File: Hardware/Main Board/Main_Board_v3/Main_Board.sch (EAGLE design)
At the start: 51 parts, among them IC1 MBED_MICROCONTROLLER, IC2 NE555, Q1 IRF3704, Q2 BS170

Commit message: Changed mounting holes and SD card Power pin
1. The mounting holes locations have been changed slightly so that they
are to the nearest mm
2. The SD card can be power gated using pin 9.
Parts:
- removed 2N7000: (no value), jumper:JP2E
- removed C2: 100nF, capacitor-wima:C5/3
- removed JP10: (no value), jumper:JP1E
- removed JP9: JP9, jumper:JP1E
- removed POWER_SUPPLY: TRACO_ISOLATED_SUPPLY, ekohub2013:TRACO_ISOLATED_SUPPLY
- removed U$2: MICROSD_SOCKET, ekohub2013:MICROSD_SOCKET
- removed U$3: PANASONIC_CR2032, Datalogging_Custom_Parts:PANASONIC_CR2032
- added C11: 100nF, capacitor-wima:C5/3.5
- added JP15, JP16, JP17, JP18, JP19, JP20: (no value), jumper:JP4E
- added JP5: (no value), jumper:JP1E
- added Q3, Q4, Q6: IRF3704L-V, transistor-power:IRF3704L-V
- added Q5: BS170, transistor-small-signal:BS170
- added R17: 20, rcl:R-EU_0411/12
- added R18: (no value), rcl:R-EU_0411/12
- added R19: 1M, rcl:R-EU_0411/12
- added R5: (no value), rcl:R-TRIMM
- added U$9: TRACO_ISOLATED_SUPPLY, ekohub2013:TRACO_ISOLATED_SUPPLY
- C1, C3, C4, C5, C6, C7, C8, C9: device capacitor-wima:C5/3 -> capacitor-wima:C5/3.5
- C10: value (none) -> 10n; device capacitor-wima:C5/3 -> capacitor-wima:C5/3.5
- DIS1: device display-lcd:TUXGR_16X2_R2 -> display-lcd3:TUXGR_16X2_R2
- JP1: value JP1 -> (none); device jumper:JP10Q -> jumper:JP2W
- JP2: value JP2 -> (none); device jumper:JP10Q -> jumper:JP2W
- JP3: value JP3 -> (none); device jumper:JP10Q -> jumper:JP4E
- JP4: value JP4 -> (none); device jumper:JP10Q -> jumper:JP4E
- Q1: value IRF3704 -> BS170; device transistor-power:IRF3704 -> transistor-small-signal:BS170
- R13, R6: value (none) -> 1M
- R4: value (none) -> 300k
- R7: value 20 -> (none)
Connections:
- removed net 5V: Q1.S, R13.2
- removed net N$10: IC1.P$10, JP1.1, JP1.2
- removed net N$13: IC1.P$13, JP2.15, JP2.16
- removed net N$14: IC1.P$14, JP2.13, JP2.14
- removed net N$23: IC1.P$38, JP4.15, JP4.16
- removed net N$24: IC1.P$37, JP4.13, JP4.14
- removed net N$35: IC1.P$26, JP3.11, JP3.12
- removed net N$36: IC1.P$25, JP3.10, JP3.9
- removed net N$45: DIS1.NC@1, R7.2
- removed net NR: IC1.P$4, JP1.13, JP1.14
- removed net P16_LCD: 2N7000.1, DIS1.NC@2
- removed net P29: IC1.P$29, IC2.TRI, JP3.17, JP3.18
- removed net P33: C3.1, IC1.P$33, JP4.5, JP4.6, R1.2, U$5.1
- removed net P34: C4.1, IC1.P$34, JP4.7, JP4.8, R14.2, U$6.1
- removed net P35: C5.1, IC1.P$35, JP4.10, JP4.9, R15.2, U$7.1
- removed net P36: IC1.P$36, JP4.11, JP4.12, Q2.G
- removed net VB: IC1.P$3, JP1.15, JP1.16, U$3.VB
- new net 3V3: JP2.1, Q6.D
- new net N$8: Q1.D, Q4.G, R6.1
- new net P10: C3.1, IC1.P$10, R1.2, U$5.1
- new net P11: C4.1, IC1.P$11, R14.2, U$6.1
- new net P12: C5.1, IC1.P$12, R15.2, U$7.1
- new net P13: C6.1, IC1.P$13, R16.2, U$8.1
- new net P14: IC1.P$14, IC2.TRI
- new net P9: IC1.P$9, Q5.G
- net 3V3_MBED: now also C11.2, Q6.S, R19.2; no longer C2.1, JP4.19, JP4.20, U$2.VDD
- net 5V_MBED: now also JP5.1; no longer C1.1, D1.A, DIS1.VCC, IC2./RES, IC2.VCC+, JP10.1, JP4.17, JP4.18, R4.2, R7.1, U$5.4, U$6.4, U$7.4, U$8.4
- net D+: no longer JP4.1, JP4.2
- net D-: no longer JP4.3, JP4.4
- net GND: now also C11.1, DIS1.NC@2, JP1.2, JP15.2, JP16.2, JP17.2, JP18.2, JP19.2, JP20.2, JP3.2, JP4.2, Q1.S, Q5.S, R5.A, R5.S, U$9.VOUT-; no longer 2N7000.3, C2.2, JP1.19, JP1.20, JP10.2, POWER_SUPPLY.VOUT-, R6.1, U$2.VSS, U$3.GND
- net MODEM: now also Q3.D; no longer Q1.D
- net N$11: now also IC2.OUT, Q1.G; no longer IC1.P$11, JP2.19, JP2.20
- net N$12: now also Q4.D, R17.2; no longer IC1.P$12, JP2.17, JP2.18
- net N$3: now also R5.E; no longer R6.2
- net N$5: now also Q3.G; no longer Q1.G
- net N$7: now also Q5.D, Q6.G, R19.1; no longer 2N7000.2, IC2.OUT
- net N$9: now also DIS1.NC@1, R17.1; no longer IC1.P$9, JP1.3, JP1.4
- net P15: no longer JP2.11, JP2.12
- net P16: no longer JP2.10, JP2.9
- net P17: no longer JP2.7, JP2.8
- net P18: no longer JP2.5, JP2.6
- net P19: no longer JP2.3, JP2.4
- net P20: no longer JP2.1, JP2.2
- net P21: no longer JP3.1, JP3.2
- net P22: no longer JP3.3, JP3.4
- net P23: no longer JP3.5, JP3.6
- net P24: no longer JP3.7, JP3.8
- net P30: now also Q2.G; no longer C6.1, JP3.19, JP3.20, R16.2, U$8.1
- net P5: now also JP2.2; no longer JP1.11, JP1.12, U$2.DI
- net P6: now also JP1.1; no longer JP1.10, JP1.9, U$2.DO
- net P7: now also JP1.3; no longer JP1.7, JP1.8, U$2.CLK
- net P8: now also JP2.3; no longer JP1.5, JP1.6, U$2.CS
- net SCL: now also JP15.4, JP16.4, JP17.4, JP18.4, JP19.4, JP20.4, JP3.4, JP4.4, R7.2; no longer JP3.13, JP3.14, JP9.2
- net SDA: now also JP15.3, JP16.3, JP17.3, JP18.3, JP19.3, JP20.3, JP3.3, JP4.3, R18.2; no longer JP3.15, JP3.16, JP9.1
- net VIN: now also C1.1, D1.A, DIS1.VCC, IC2./RES, IC2.VCC+, JP15.1, JP16.1, JP17.1, JP18.1, JP19.1, JP20.1, JP3.1, JP4.1, JP5.2, Q3.S, Q4.S, R13.2, R18.1, R4.2, R6.2, R7.1, U$5.4, U$6.4, U$7.4, U$8.4, U$9.VOUT+; no longer JP1.17, JP1.18, POWER_SUPPLY.VOUT+
- net VIN+: now also U$9.VIN1+, U$9.VIN2+; no longer POWER_SUPPLY.VIN1+, POWER_SUPPLY.VIN2+
- net VIN-: now also U$9.VIN1-, U$9.VIN2-; no longer POWER_SUPPLY.VIN1-, POWER_SUPPLY.VIN2-
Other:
- note added: "The 5V_MBED will only be powered when the USB is on"
- note added: "make holes for switches bigger"
- moved on the sheet: C1, C10, C3, C4, C5, C6, C7, C8, C9, D1, D2, D3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

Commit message: Added power control of the LCD screen
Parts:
- added Q7: BS170, transistor-small-signal:BS170
- added Q8: IRF3704L-V, transistor-power:IRF3704L-V
- added R20: 1M, rcl:R-EU_0411/12
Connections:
- new net N$10: Q7.D, Q8.G, R20.1
- new net P25: IC1.P$25, Q7.G
- new net VIN_LCD: C1.1, DIS1.VCC, Q8.D
- net GND: now also Q7.S
- net VIN: now also Q8.S, R20.2; no longer C1.1, DIS1.VCC
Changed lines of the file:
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@@
 <part name="SUPPLY8" library="supply2" deviceset="GND" device=""/>
 <part name="Q6" library="transistor-power" deviceset="IRF3704" device="L-V"/>
+<part name="Q7" library="transistor-small-signal" deviceset="BS170" device=""/>
+<part name="R20" library="rcl" deviceset="R-EU_" device="0411/12" value="1M"/>
+<part name="SUPPLY12" library="supply2" deviceset="GND" device=""/>
+<part name="Q8" library="transistor-power" deviceset="IRF3704" device="L-V"/>
 </parts>
 <sheets>
@@
 <instance part="SUPPLY8" gate="GND" x="163.83" y="-76.2"/>
 <instance part="Q6" gate="G$1" x="166.37" y="-44.45" rot="MR90"/>
+<instance part="Q7" gate="1" x="-123.19" y="-88.9"/>
+<instance part="R20" gate="G$1" x="-137.16" y="-73.66" rot="R90"/>
+<instance part="SUPPLY12" gate="GND" x="-120.65" y="-101.6"/>
+<instance part="Q8" gate="G$1" x="-118.11" y="-69.85" rot="MR90"/>
 </instances>
 <busses>
@@
 <pinref part="SUPPLY8" gate="GND" pin="GND"/>
 </segment>
+<segment>
+<pinref part="Q7" gate="1" pin="S"/>
+<wire x1="-120.65" y1="-93.98" x2="-120.65" y2="-99.06" width="0.1524" layer="91"/>
+<pinref part="SUPPLY12" gate="GND" pin="GND"/>
+</segment>
 </net>
 <net name="VIN" class="0">
@@
 <label x="76.2" y="-33.02" size="1.4224" layer="95" rot="R180"/>
 <pinref part="Q3" gate="G$1" pin="S"/>
-</segment>
-<segment>
-<wire x1="-71.12" y1="-63.5" x2="-71.12" y2="-67.31" width="0.1524" layer="91"/>
-<label x="-79.375" y="-65.405" size="0.8128" layer="95" rot="R180"/>
-<pinref part="DIS1" gate="G$1" pin="VCC"/>
-<wire x1="-71.12" y1="-67.31" x2="-80.01" y2="-67.31" width="0.1524" layer="91"/>
-<pinref part="C1" gate="G$1" pin="1"/>
-<wire x1="-80.01" y1="-67.31" x2="-80.01" y2="-82.55" width="0.1524" layer="91"/>
 </segment>
 <segment>
@@
 <wire x1="83.82" y1="20.32" x2="77.47" y2="20.32" width="0.1524" layer="91"/>
 <wire x1="77.47" y1="20.32" x2="77.47" y2="16.51" width="0.1524" layer="91"/>
+</segment>
+<segment>
+<wire x1="-123.19" y1="-67.31" x2="-137.16" y2="-67.31" width="0.1524" layer="91"/>
+<pinref part="R20" gate="G$1" pin="2"/>
+<wire x1="-137.16" y1="-67.31" x2="-146.05" y2="-67.31" width="0.1524" layer="91"/>
+<wire x1="-137.16" y1="-68.58" x2="-137.16" y2="-67.31" width="0.1524" layer="91"/>
+<junction x="-137.16" y="-67.31"/>
+<label x="-142.24" y="-64.77" size="1.4224" layer="95" rot="R180"/>
+<pinref part="Q8" gate="G$1" pin="S"/>
 </segment>
 </net>
@@
 </segment>
 </net>
+<net name="N$10" class="0">
+<segment>
+<pinref part="Q7" gate="1" pin="D"/>
+<wire x1="-120.65" y1="-72.39" x2="-120.65" y2="-81.28" width="0.1524" layer="91"/>
+<pinref part="Q8" gate="G$1" pin="G"/>
+<pinref part="R20" gate="G$1" pin="1"/>
+<wire x1="-120.65" y1="-81.28" x2="-120.65" y2="-83.82" width="0.1524" layer="91"/>
+<wire x1="-137.16" y1="-78.74" x2="-137.16" y2="-81.28" width="0.1524" layer="91"/>
+<wire x1="-137.16" y1="-81.28" x2="-120.65" y2="-81.28" width="0.1524" layer="91"/>
+<junction x="-120.65" y="-81.28"/>
+</segment>
+</net>
+<net name="VIN_LCD" class="0">
+<segment>
+<wire x1="-71.12" y1="-63.5" x2="-71.12" y2="-67.31" width="0.1524" layer="91"/>
+<label x="-79.375" y="-65.405" size="0.8128" layer="95" rot="R180"/>
+<pinref part="DIS1" gate="G$1" pin="VCC"/>
+<wire x1="-71.12" y1="-67.31" x2="-80.01" y2="-67.31" width="0.1524" layer="91"/>
+<pinref part="C1" gate="G$1" pin="1"/>
+<wire x1="-80.01" y1="-67.31" x2="-80.01" y2="-82.55" width="0.1524" layer="91"/>
+<pinref part="Q8" gate="G$1" pin="D"/>
+<wire x1="-80.01" y1="-67.31" x2="-113.03" y2="-67.31" width="0.1524" layer="91"/>
+<junction x="-80.01" y="-67.31"/>
+</segment>
+</net>
+<net name="P25" class="0">
+<segment>
+<pinref part="Q7" gate="1" pin="G"/>
+<wire x1="-128.27" y1="-88.9" x2="-135.89" y2="-88.9" width="0.1524" layer="91"/>
+<label x="-135.89" y="-90.805" size="1.4224" layer="95"/>
+</segment>
+<segment>
+<pinref part="IC1" gate="G$1" pin="P$25"/>
+<wire x1="19.05" y1="-12.7" x2="35.56" y2="-12.7" width="0.1524" layer="91"/>
+<label x="36.83" y="-12.7" size="1.778" layer="95"/>
+</segment>
+</net>

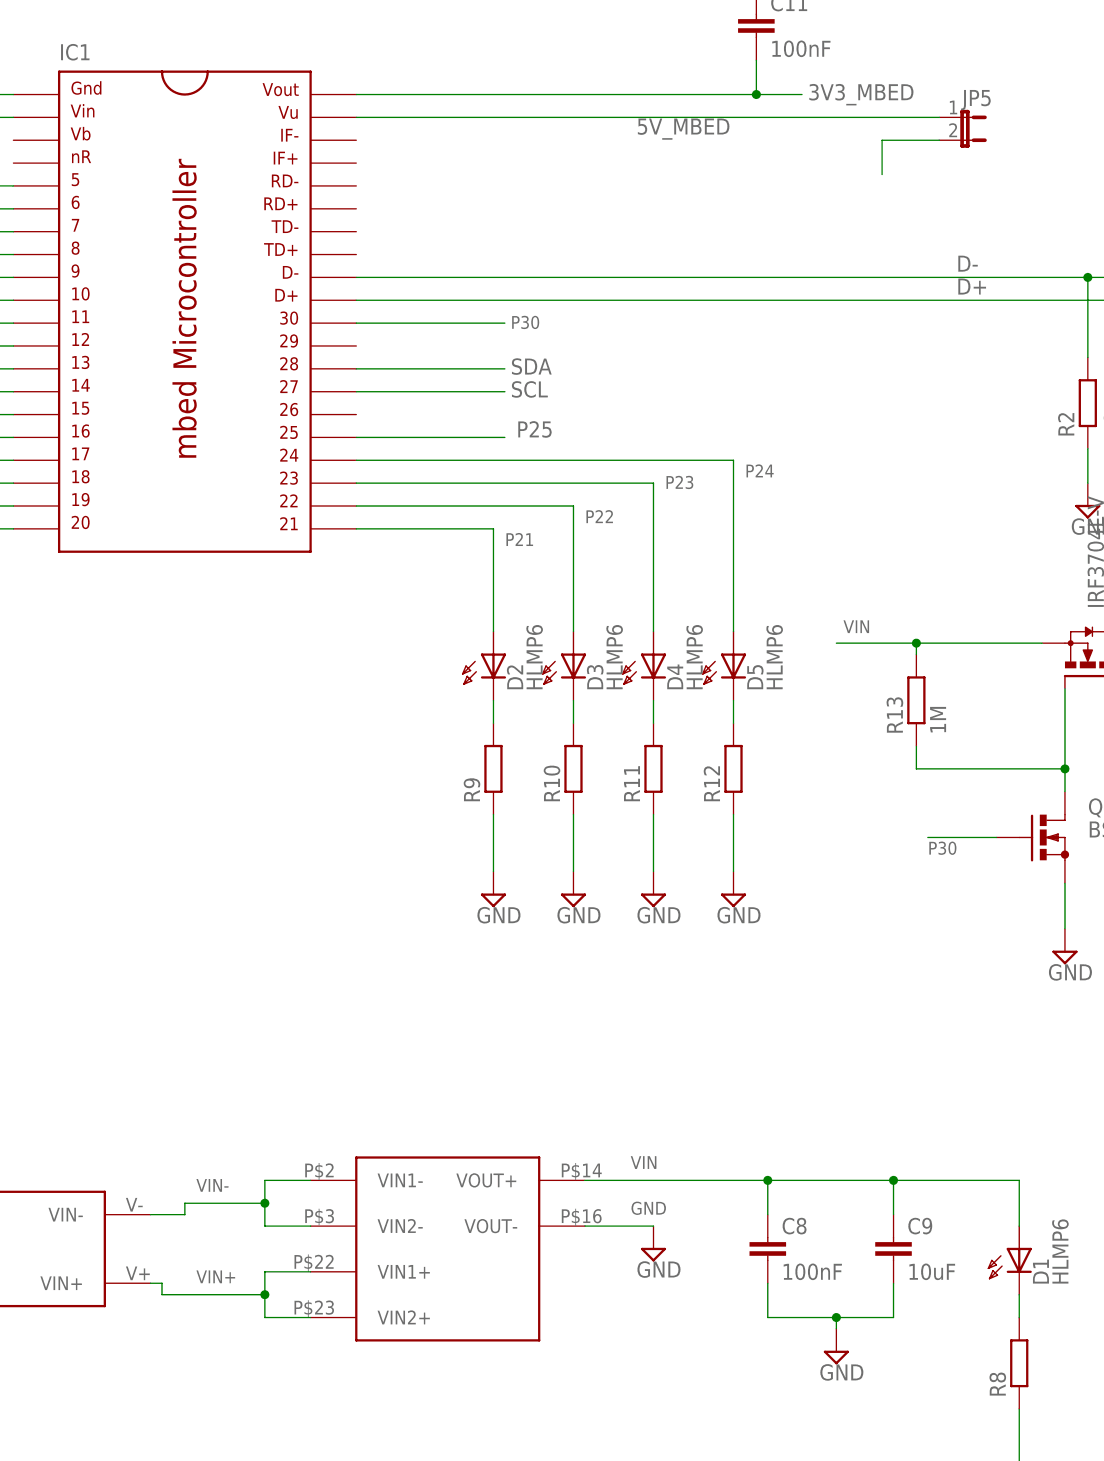
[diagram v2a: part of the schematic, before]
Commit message: Added Reverse Polarity Protection
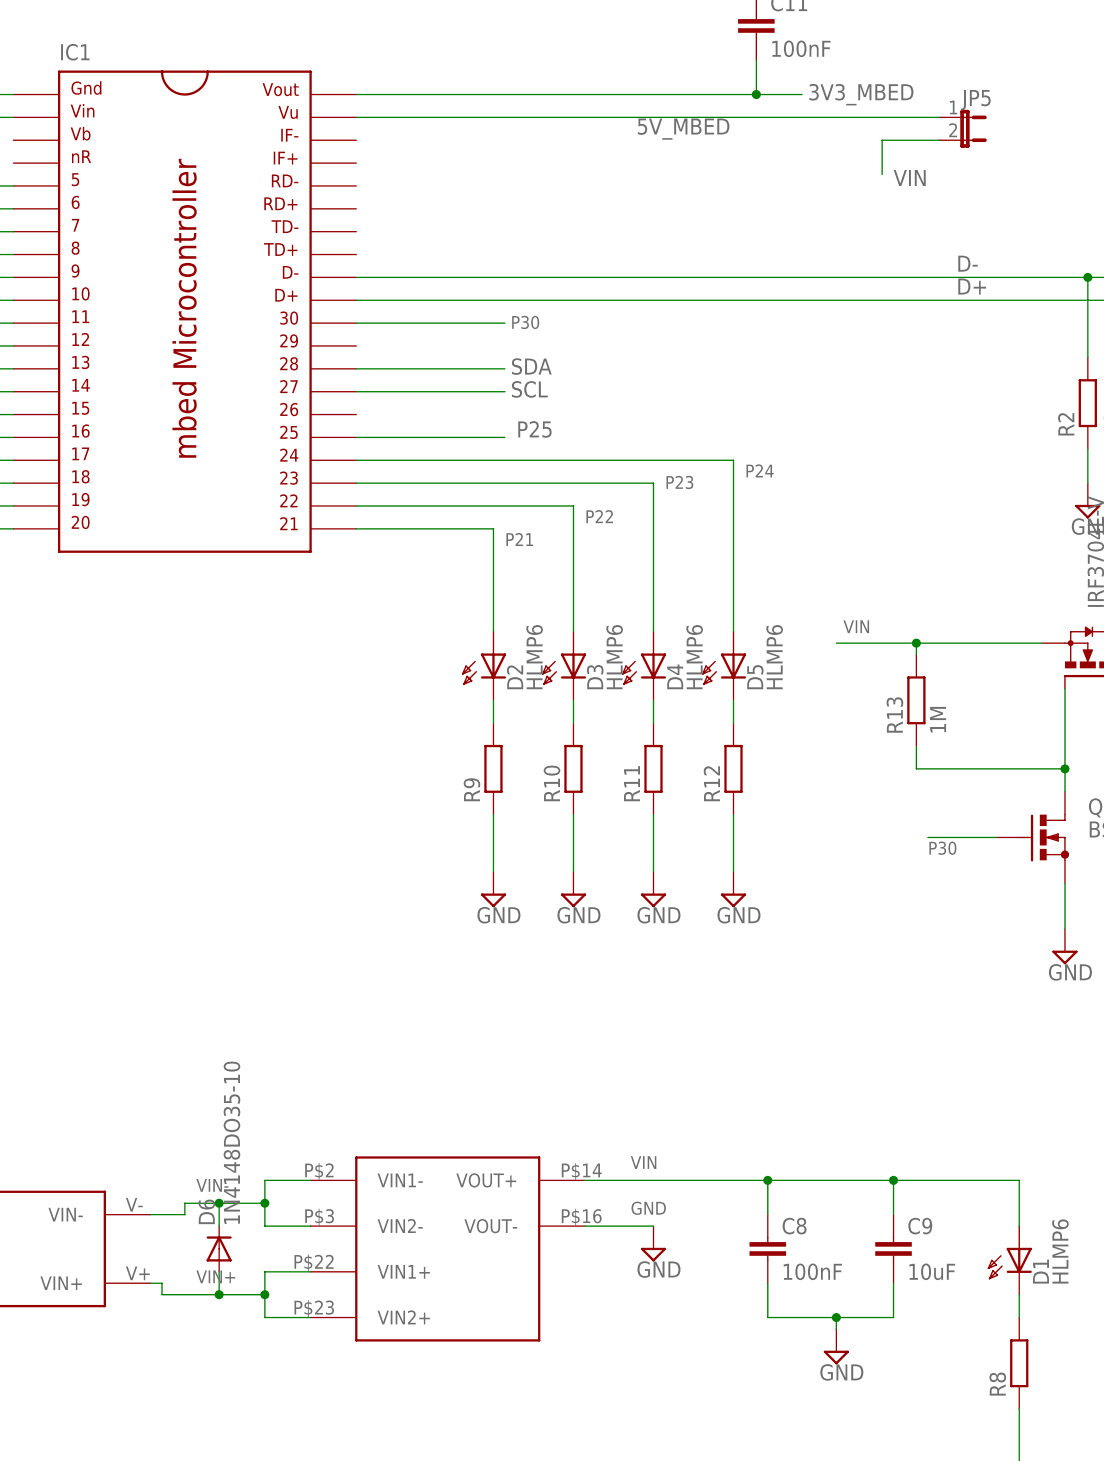
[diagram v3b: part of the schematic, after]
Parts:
- added D6: 1N4148DO35-10, diode:1N4148DO35-10
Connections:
- net VIN+: now also D6.A
- net VIN-: now also D6.C
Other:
- note removed: "The 5V_MBED will only be powered when the USB is on"
- note removed: "make holes for switches bigger"
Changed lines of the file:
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@@
 <setting verticaltext="up"/>
 </settings>
-<grid distance="0.05" unitdist="inch" unit="inch" style="lines" multiple="1" display="no" altdistance="0.025" altunitdist="inch" altunit="inch"/>
+<grid distance="0.05" unitdist="inch" unit="inch" style="lines" multiple="1" display="yes" altdistance="0.025" altunitdist="inch" altunit="inch"/>
 <layers>
 <layer number="1" name="Top" color="4" fill="1" visible="no" active="no"/>
@@
 <part name="SUPPLY12" library="supply2" deviceset="GND" device=""/>
 <part name="Q8" library="transistor-power" deviceset="IRF3704" device="L-V"/>
+<part name="D6" library="diode" deviceset="1N4148" device="DO35-10"/>
 </parts>
 <sheets>
 <sheet>
 <plain>
-<text x="-27.94" y="36.83" size="1.778" layer="98">The 5V_MBED will only be powered when the USB is on </text>
-<text x="-153.67" y="-33.02" size="1.778" layer="98">make holes for switches bigger</text>
 </plain>
 <instances>
@@
 <instance part="SUPPLY12" gate="GND" x="-120.65" y="-101.6"/>
 <instance part="Q8" gate="G$1" x="-118.11" y="-69.85" rot="MR90"/>
+<instance part="D6" gate="G$1" x="3.81" y="-102.87" rot="R90"/>
 </instances>
 <busses>
@@
 <wire x1="83.82" y1="20.32" x2="77.47" y2="20.32" width="0.1524" layer="91"/>
 <wire x1="77.47" y1="20.32" x2="77.47" y2="16.51" width="0.1524" layer="91"/>
+<label x="78.74" y="15.24" size="1.778" layer="95"/>
 </segment>
 <segment>
@@
 <wire x1="8.89" y1="-97.79" x2="8.89" y2="-95.25" width="0.1524" layer="91"/>
 <wire x1="8.89" y1="-95.25" x2="13.97" y2="-95.25" width="0.1524" layer="91"/>
-<wire x1="8.89" y1="-97.79" x2="0" y2="-97.79" width="0.1524" layer="91"/>
+<wire x1="8.89" y1="-97.79" x2="3.81" y2="-97.79" width="0.1524" layer="91"/>
 <junction x="8.89" y="-97.79"/>
 <label x="1.27" y="-96.52" size="1.4224" layer="95"/>
 <pinref part="U$9" gate="G$1" pin="VIN1-"/>
 <pinref part="U$9" gate="G$1" pin="VIN2-"/>
+<pinref part="D6" gate="G$1" pin="C"/>
+<wire x1="3.81" y1="-97.79" x2="0" y2="-97.79" width="0.1524" layer="91"/>
+<wire x1="3.81" y1="-100.33" x2="3.81" y2="-97.79" width="0.1524" layer="91"/>
+<junction x="3.81" y="-97.79"/>
 </segment>
 </net>
@@
 <wire x1="8.89" y1="-107.95" x2="8.89" y2="-110.49" width="0.1524" layer="91"/>
 <wire x1="13.97" y1="-110.49" x2="8.89" y2="-110.49" width="0.1524" layer="91"/>
-<wire x1="8.89" y1="-107.95" x2="-2.54" y2="-107.95" width="0.1524" layer="91"/>
+<wire x1="8.89" y1="-107.95" x2="3.81" y2="-107.95" width="0.1524" layer="91"/>
 <junction x="8.89" y="-107.95"/>
 <label x="1.27" y="-106.68" size="1.4224" layer="95"/>
 <pinref part="U$9" gate="G$1" pin="VIN1+"/>
 <pinref part="U$9" gate="G$1" pin="VIN2+"/>
-</segment>
-</net>
+<pinref part="D6" gate="G$1" pin="A"/>
+<wire x1="3.81" y1="-107.95" x2="-2.54" y2="-107.95" width="0.1524" layer="91"/>
+<wire x1="3.81" y1="-107.95" x2="3.81" y2="-105.41" width="0.1524" layer="91"/>
+<junction x="3.81" y="-107.95"/>
+</segment>
+</net>
